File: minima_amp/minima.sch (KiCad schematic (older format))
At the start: 40 parts, among them J1 input, J2 output, J3 powersupply, U1 LM1875

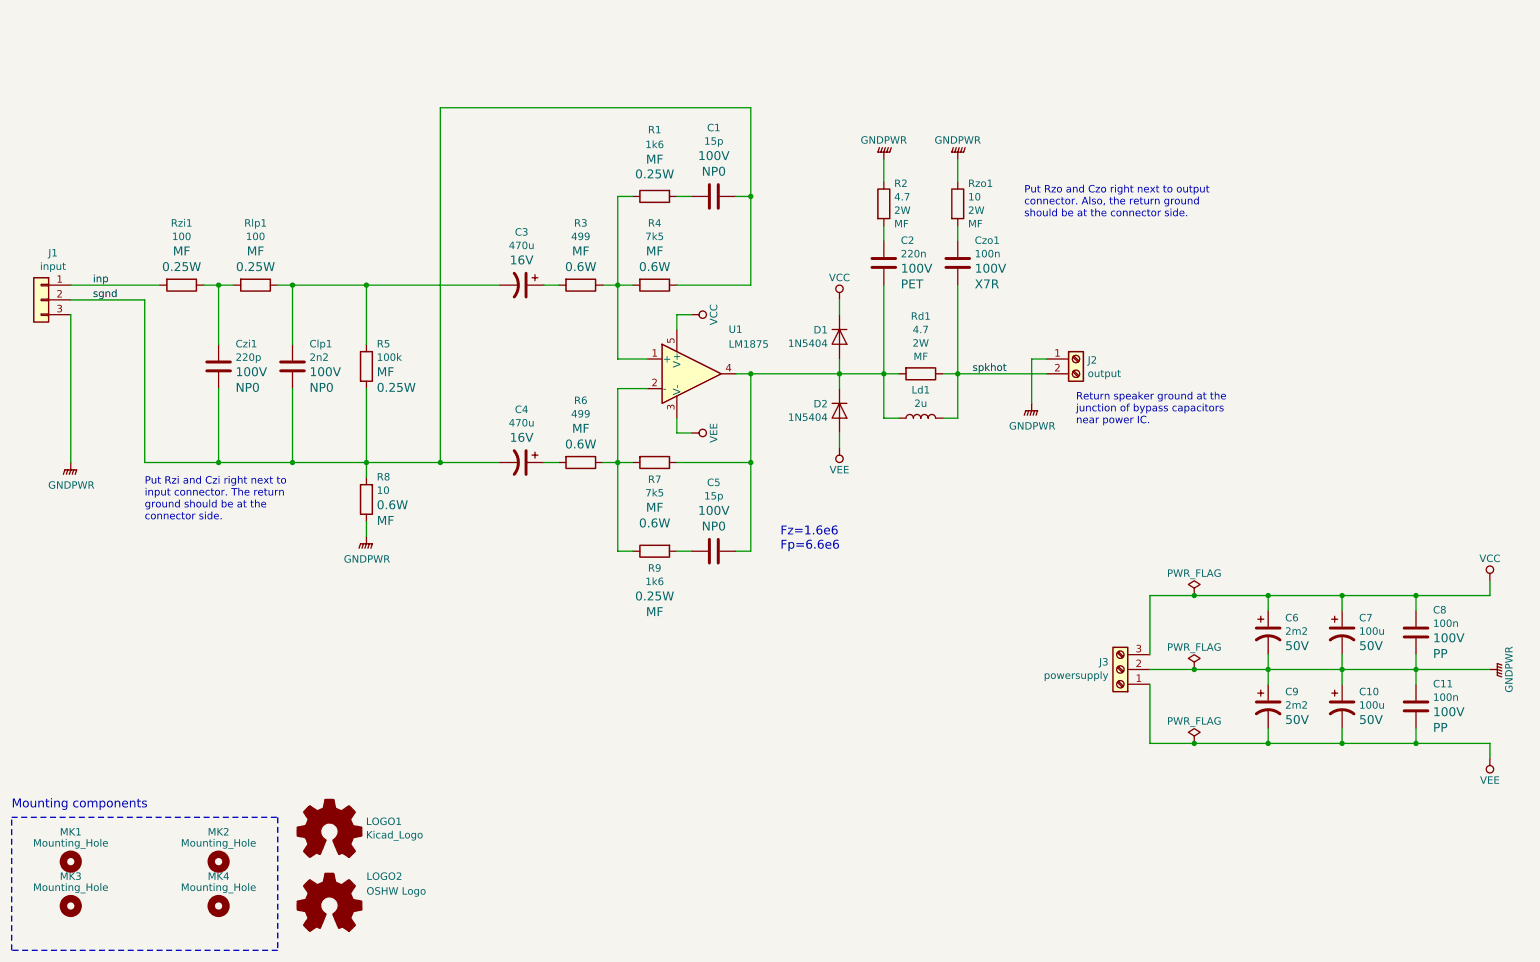
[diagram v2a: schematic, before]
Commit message: Added comments about connectors
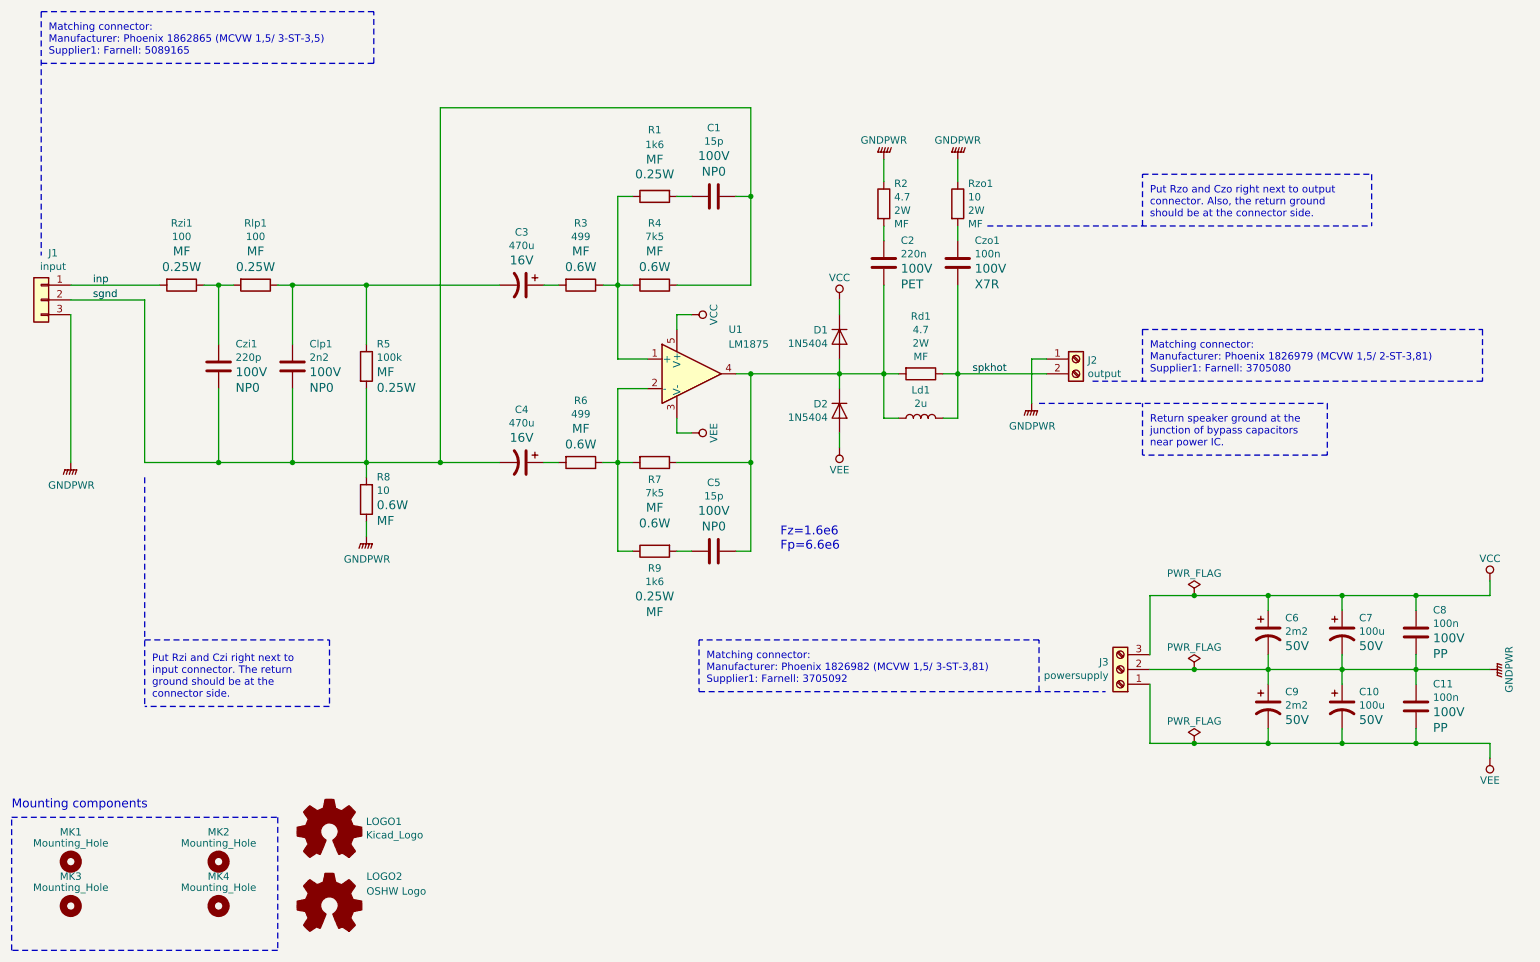
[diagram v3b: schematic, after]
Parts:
- J1: Manufacturer Phoenix:1843619 -> Phoenix: 1843619 (MCV 1,5/ 3-G-3,81); Vendor Farnell:3704828 -> Farnell: 3704828
- J2: Manufacturer Phoenix:MCV 1,5/ 2-GF-3,81 -> Phoenix: 1803426 (MCV 1,5/ 2-G-3,81); Vendor Farnell:1793055 -> Farnell: 3913077
- J3: Manufacturer Phoenix:1803439 -> Phoenix: 1803439 (MCV 1,5/ 3-G-3,81); Vendoe (none) -> Farnell: 3913089; Vendor Farnell:3913089 -> (none)
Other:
- note added: "Matching connector:\nManufacturer: Phoenix 1826979 (MCVW 1,5/ 2-ST-3,81)\nSupplier1: Farnell: 3705080"
- note added: "Matching connector:\nManufacturer: Phoenix 1826982 (MCVW 1,5/ 3-ST-3,81)\nSupplier1: Farnell: 3705092"
- note added: "Matching connector:\nManufacturer: Phoenix 1862865 (MCVW 1,5/ 3-ST-3,5)\nSupplier1: Farnell: 5089165"
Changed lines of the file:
@@
 F 2 "Connector_Phoenix_MC:PhoenixContact_MCV_1,5_2-G-3.81_1x02_P3.81mm_Vertical" H 8000 3500 50  0001 C CNN
 F 3 "http://www.farnell.com/datasheets/2133308.pdf" H 8000 3500 50  0001 C CNN
-F 4 "Farnell:1793055" H 8000 3500 60  0001 C CNN "Vendor"
-F 5 "Phoenix:MCV 1,5/ 2-GF-3,81 " H 8000 3500 60  0001 C CNN "Manufacturer"
+F 4 "Farnell: 3913077" H 8000 3500 60  0001 C CNN "Vendor"
+F 5 "Phoenix: 1803426 (MCV 1,5/ 2-G-3,81)" H 8000 3500 60  0001 C CNN "Manufacturer"
 	1    8000 3500
 	1    0    0    -1
@@
 F 2 "Connector_Phoenix_MC:PhoenixContact_MCV_1,5_3-G-3.5_1x03_P3.50mm_Vertical" H 1000 3100 50  0001 C CNN
 F 3 "http://www.farnell.com/datasheets/2309782.pdf" H 1000 3100 50  0001 C CNN
-F 4 "Phoenix:1843619" H -1500 1200 50  0001 C CNN "Manufacturer"
-F 5 "Farnell:3704828" H -1500 1200 50  0001 C CNN "Vendor"
+F 4 "Phoenix: 1843619 (MCV 1,5/ 3-G-3,81)" H -1500 1200 50  0001 C CNN "Manufacturer"
+F 5 "Farnell: 3704828" H -1500 1200 50  0001 C CNN "Vendor"
 	1    1000 3100
 	-1   0    0    -1
@@
 F 2 "Connector_Phoenix_MC:PhoenixContact_MCV_1,5_3-G-3.81_1x03_P3.81mm_Vertical" H 8300 5600 50  0001 C CNN
 F 3 "http://www.farnell.com/datasheets/2138271.pdf" H 8300 5600 50  0001 C CNN
-F 4 "Phoenix:1803439" H 2750 1300 50  0001 C CNN "Manufacturer"
-F 5 "Farnell:3913089" H 2750 1300 50  0001 C CNN "Vendor"
+F 4 "Phoenix: 1803439 (MCV 1,5/ 3-G-3,81)" H 2750 1300 50  0001 C CNN "Manufacturer"
+F 5 "Farnell: 3913089" H 2750 1300 50  0001 C CNN "Vendoe"
 	1    8300 5600
 	-1   0    0    1
@@
 	1    0    0    -1
 $EndComp
-Text Notes 8000 3950 0    50   ~ 0
+Text Notes 8500 4100 0    50   ~ 0
 Return speaker ground at the\njunction of bypass capacitors \nnear power IC.
 $Comp
@@
 	1    0    0    -1
 $EndComp
-Text Notes 1700 4600 0    50   ~ 0
+Text Notes 1750 5800 0    50   ~ 0
 Put Rzi and Czi right next to\ninput connector. The return\nground should be at the\nconnector side.
 Text Label 1350 3100 0    50   ~ 0
@@
 Wire Wire Line
 	7200 2600 7200 2700
-Text Notes 7650 2550 0    50   ~ 0
+Text Notes 8500 2550 0    50   ~ 0
 Put Rzo and Czo right next to output \nconnector. Also, the return ground \nshould be at the connector side.
 Wire Wire Line
@@
 Text Label 7300 3600 0    50   ~ 0
 spkhot
+Text Notes 8500 3600 0    50   ~ 0
+Matching connector:\nManufacturer: Phoenix 1826979 (MCVW 1,5/ 2-ST-3,81)\nSupplier1: Farnell: 3705080
+Wire Notes Line
+	9700 3800 9700 4150
+Wire Notes Line
+	9700 4150 8450 4150
+Wire Notes Line
+	8450 4150 8450 3800
+Wire Notes Line
+	7750 3800 9700 3800
+Wire Notes Line
+	8450 2250 10000 2250
+Wire Notes Line
+	10000 2250 10000 2600
+Wire Notes Line
+	8450 2600 8450 2250
+Wire Notes Line
+	7400 2600 10000 2600
+Wire Notes Line
+	1700 5400 2950 5400
+Wire Notes Line
+	2950 5400 2950 5850
+Wire Notes Line
+	2950 5850 1700 5850
+Text Notes 5500 5700 0    50   ~ 0
+Matching connector:\nManufacturer: Phoenix 1826982 (MCVW 1,5/ 3-ST-3,81)\nSupplier1: Farnell: 3705092
+Wire Notes Line
+	8450 3300 10750 3300
+Wire Notes Line
+	10750 3300 10750 3650
+Wire Notes Line
+	10750 3650 8100 3650
+Wire Notes Line
+	8450 3300 8450 3650
+Wire Notes Line
+	7750 5750 7750 5400
+Wire Notes Line
+	7750 5400 5450 5400
+Wire Notes Line
+	5450 5400 5450 5750
+Wire Notes Line
+	5450 5750 8200 5750
+Text Notes 1050 1450 0    50   ~ 0
+Matching connector:\nManufacturer: Phoenix 1862865 (MCVW 1,5/ 3-ST-3,5)\nSupplier1: Farnell: 5089165
+Wire Notes Line
+	1000 1500 3250 1500
+Wire Notes Line
+	3250 1500 3250 1150
+Wire Notes Line
+	3250 1150 1000 1150
+Wire Notes Line
+	1000 1150 1000 2800
+Wire Notes Line
+	1700 4300 1700 5850
 $EndSCHEMATC
